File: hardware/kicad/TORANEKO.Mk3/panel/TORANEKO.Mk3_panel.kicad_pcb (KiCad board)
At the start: 2 copper layers, 60 x 56.3 mm, 21 parts, among them IC5 AS5047P-ATSM, IC5_2 AS5047P-ATSM, IC5_3 AS5047P-ATSM, IC7 AS5047P-ATSM, IC7_2 AS5047P-ATSM, IC7_3 AS5047P-ATSM, U3 Encord, U3_2 Encord, U3_3 Encord, U5 Encord, U5_2 Encord, U5_3 Encord

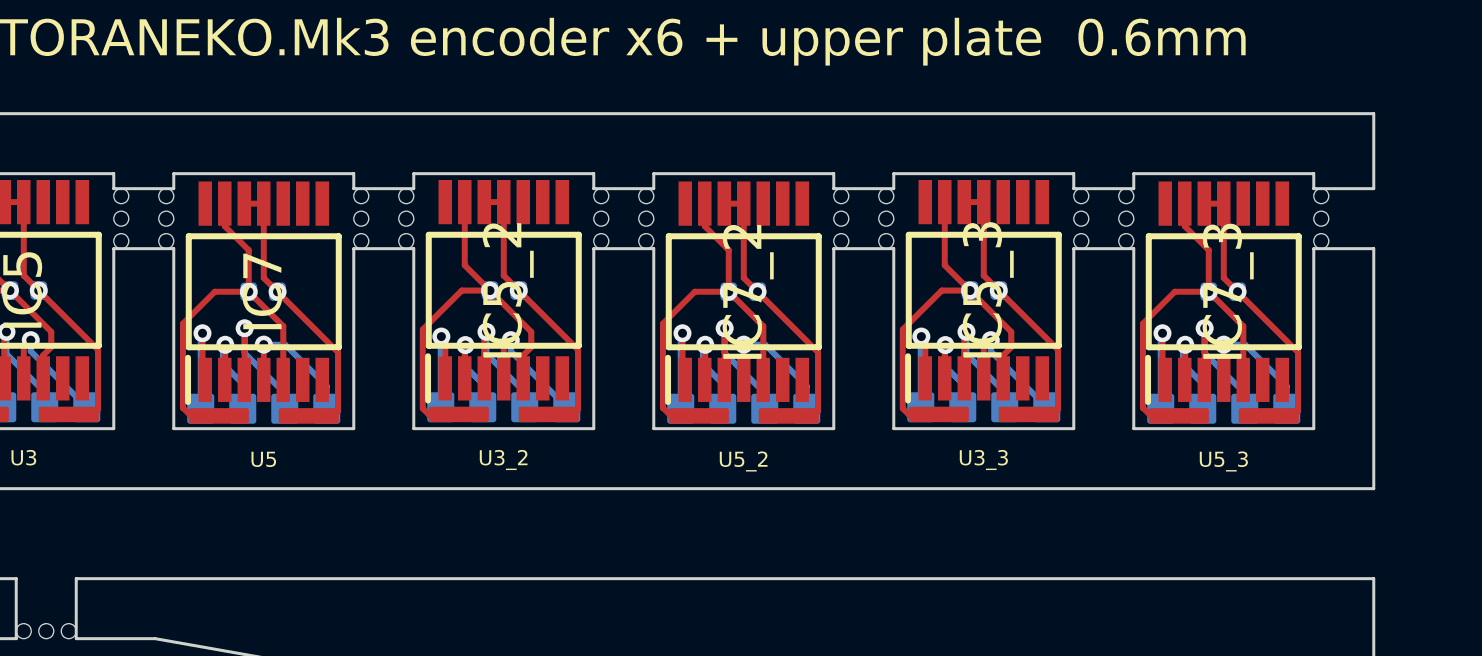
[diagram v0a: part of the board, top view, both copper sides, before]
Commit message: Main PCB check fixes: encoder B edge gap, via spacing, fine-pitch DRC rule
- Move encoder board B outline down 0.05mm so U5 pads are 0.213mm from
  the edge (same as U3; was 0.163mm). Panel regenerated to match.
- Nudge VBAT via at (102.15, 82.65) to (102.1, 82.7): hole gap 0.195 -> 0.27mm
- Add TORANEKO.Mk3.kicad_dru allowing 0.14mm between pads of U1 (LGA-14)
  and IC6 (UFQFPN48), whose footprints are 0.15-0.18mm apart by design

Co-Authored-By: Claude Opus 5.5 <noreply@anthropic.com>
Claude-Session: https://claude.ai/code/session_01Cv6KpZe6NLHWQTjQMUz9Sg
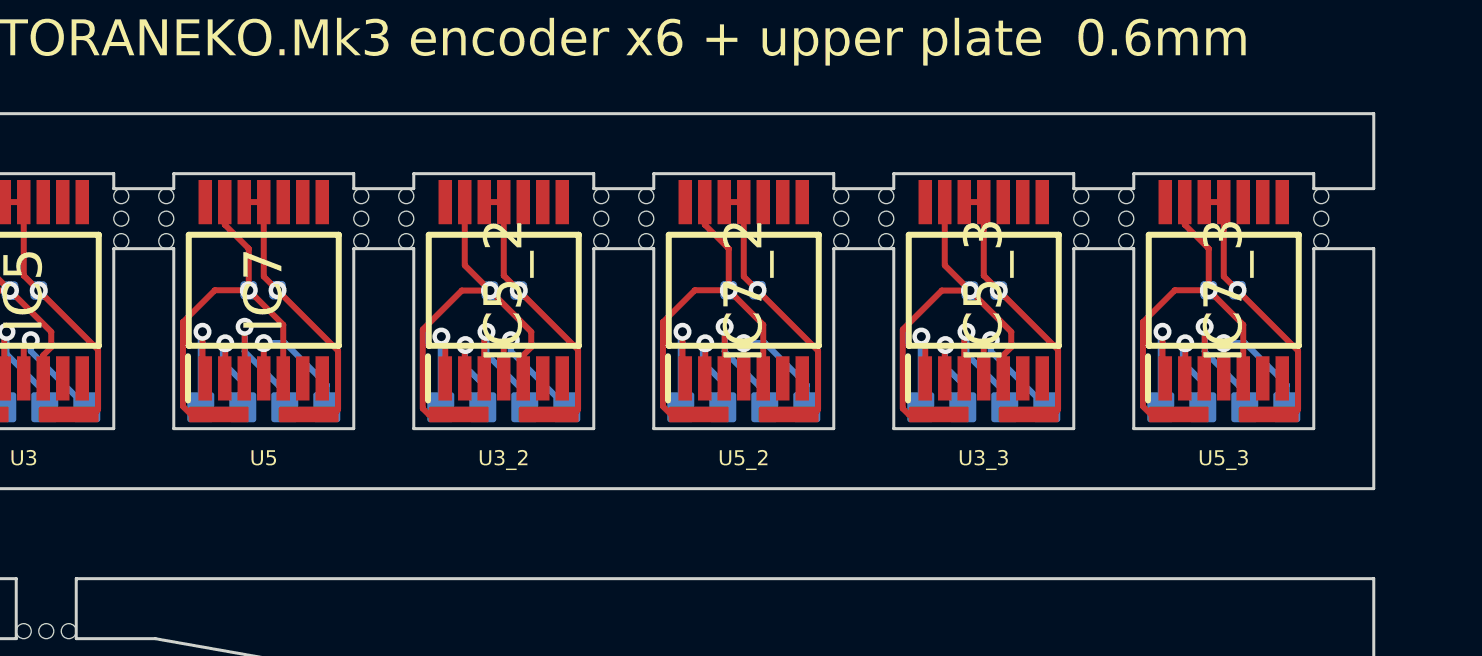
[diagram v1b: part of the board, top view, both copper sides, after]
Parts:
- moved U5 0.05 mm to (118.0, 115.5)
- moved U5_2 0.05 mm to (134.0, 115.5)
- moved U5_3 0.05 mm to (150.0, 115.5)
